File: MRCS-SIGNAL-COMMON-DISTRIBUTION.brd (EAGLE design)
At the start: 69 x 50 mm, 13 parts, among them CON1 DC PWR, CON2 DC PWR

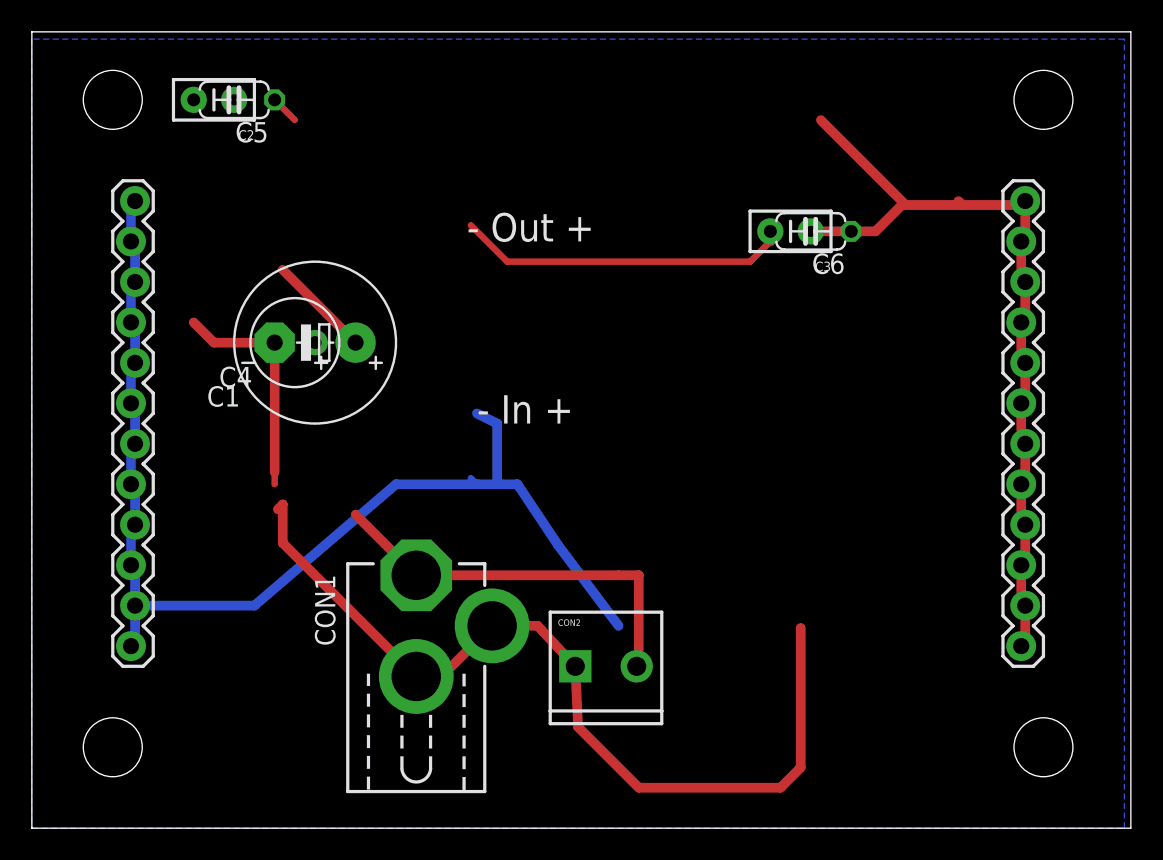
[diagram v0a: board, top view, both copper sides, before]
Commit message: initial board for testing
first pass, this is based on the Buckeroo footprint
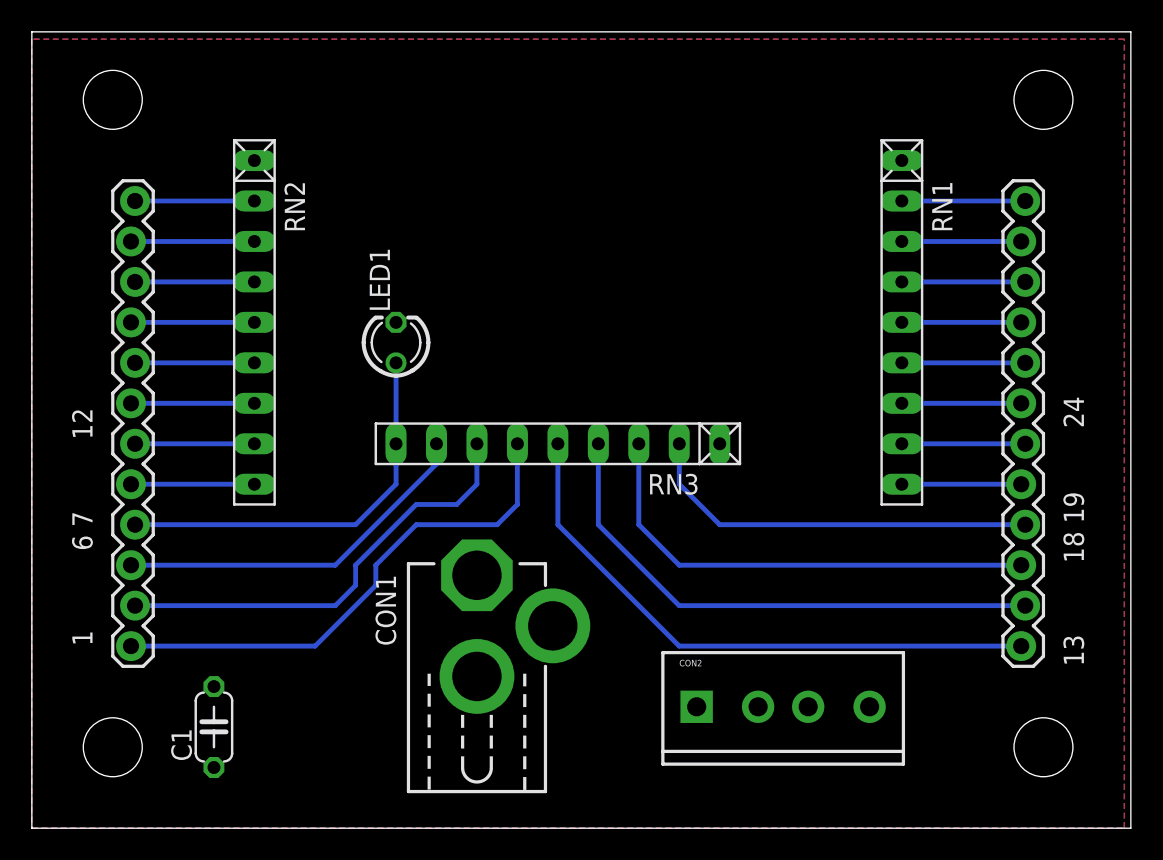
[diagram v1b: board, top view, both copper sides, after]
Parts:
- removed C2: 1.0uF@50, SPCoast:C-PTH-0.100
- removed C3: 10uF@50, SPCoast:C-PTH-0.100
- removed C4: 220uF @ 35V, SPCoast:E2.5-6
- removed C5: 1.0 UF@ 50V, SPCoast:C050-024X044
- removed C6: 10uF @ 50V, SPCoast:C050-024X044
- removed OUTPUT+: OUTPUT+, SPCoast:1X12_LOCK
- removed U$1: (no value), MRCS-prop65warningBtm:CA-PROP65WARNING
- removed U$3: (no value), MRCSLogoBtm:MRCSLOGOBTM
- added CON3: OUTPUT1, SPCoast:1X12_LOCK
- added LED1: RED, SPCoast:LED3MM
- added RN1, RN2, RN3: 270, resistor-net:RN-9
- C1: value 150uF@50 -> .01 uF; device SPCoast:E5-10.5 -> SPCoast:C050-024X044
- CON2: value DC PWR -> Power/GND; device SPCoast:SCREWTERMINAL-3.5MM-2_LOCK -> SPCoast:SCREWTERMINAL-3.5MM-4_LOCK
- CON4: value OUTPUT- -> OUTPUT2
- moved U$2 48.6 mm to (40.6, 39.4)
- moved C1 25.0 mm to (11.4, 6.35), turned to 90 degrees
- moved CON2 8.03 mm to (41.9, 7.62)
- moved CON1 3.81 mm to (27.9, 12.7)
- renumbered OUTPUT- to CON4
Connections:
- removed net OUTPUT+: C3.1, OUTPUT+.1, OUTPUT+.10, OUTPUT+.11, OUTPUT+.12, OUTPUT+.2, OUTPUT+.3, OUTPUT+.4, OUTPUT+.5, OUTPUT+.6, OUTPUT+.7, OUTPUT+.8, OUTPUT+.9
- new net N$10: CON4.11, RN2.3
- new net N$11: CON4.10, RN2.4
- new net N$12: CON4.9, RN2.5
- new net N$13: CON4.8, RN2.6
- new net N$14: CON4.7, RN2.7
- new net N$15: CON4.6, RN2.8
- new net N$16: CON4.5, RN2.9
- new net N$17: CON3.4, RN3.2
- new net N$18: CON3.3, RN3.3
- new net N$19: CON3.2, RN3.4
- new net N$20: CON3.1, RN3.5
- new net N$21: CON4.1, RN3.6
- new net N$22: CON4.4, LED1.A, RN3.9
- new net N$23: CON4.3, RN3.8
- new net N$24: CON4.2, RN3.7
- new net N$7: CON3.6, RN1.8
- net GND: now also C1.2, CON2.3, LED1.K; no longer C1.-, C3.2, CON4.1, CON4.10, CON4.11, CON4.12, CON4.2, CON4.3, CON4.4, CON4.5, CON4.6, CON4.7, CON4.8, CON4.9
- net INPUT+: now also C1.1, CON2.4, RN1.1, RN2.1
- net N$1: now also CON3.12, RN1.2; no longer C5.1
- net N$2: now also CON3.11, RN1.3; no longer C4.+
- net N$3: now also CON3.10, RN1.4; no longer C1.+
- net N$4: now also CON3.9, RN1.5; no longer C2.2
- net N$5: now also CON3.8, RN1.6; no longer C4.-
- net N$6: now also CON3.7, RN1.7; no longer C5.2
- net N$8: now also CON3.5, RN1.9; no longer C6.2
- net N$9: now also CON4.12, RN2.2; no longer C6.1
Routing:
- net GND: track 171.9 -> 0.00 mm
- net OUTPUT+: track 51.3 -> 0.00 mm
- net N$20: track 0.00 -> 37.3 mm
- net N$19: track 0.00 -> 34.0 mm
- net N$21: track 0.00 -> 32.5 mm
- net N$18: track 0.00 -> 30.3 mm
- net N$24: track 0.00 -> 27.9 mm
- net INPUT+: track 26.0 -> 0.00 mm
- net N$17: track 0.00 -> 25.3 mm
- net N$22: track 0.00 -> 25.1 mm
- net N$23: track 0.00 -> 23.1 mm
- net N$16: track 0.00 -> 7.75 mm
- net N$14: track 0.00 -> 7.75 mm
- net N$12: track 0.00 -> 7.75 mm
- net N$10: track 0.00 -> 7.75 mm
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- added copper zone on layer 16, net GND
- added copper zone on layer 1, net INPUT+
- removed copper zone on layer 16, net OUTOUT-
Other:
- board text added: "1 6 7 12"
- board text added: "13 18 19 24"
- board text added: "G + G +"
- board text added: "Signal Common Distribution Seth Neumann 20240126 V 1.0"
- board text removed: ""Buckeroo V1.6" Seth Neumann 20230226"
- board text removed: "+ V Jumper"
- board text removed: "- In +"
- board text removed: "- Out +"
- board text removed: "- V (GND) JUMP"
- board text removed: "C1"
- board text removed: "C2"
- board text removed: "C3"
- board text removed: "C4"
- board text removed: "C5"
- board text removed: "C6"
- board text removed: "CON1"
- board text removed: "CON2"
- board text removed: "GND"
- board text removed: "IN - +"
- board text removed: "MH-MINI-360"
- board text removed: "Output +"
- board text removed: "Output -"
- board text removed: "U$4"
- board text removed: "U$5"
- board text removed: "VR1"

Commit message: last minute fixes
added Prop 65 label and bottom logo
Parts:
- added U$1: (no value), MRCS-prop65warningBtm:CA-PROP65WARNING
- added U$3: (no value), MRCSLogoBtm:MRCSLOGOBTM
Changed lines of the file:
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@@
 <attribute name="NAME" x="15.875" y="40.64" size="1.27" layer="25" ratio="10" rot="R270"/>
 </element>
+<element name="U$1" library="MRCS-prop65warningBtm" package="CA-PROP65WARNING" value="" x="40.64" y="39.37"/>
+<element name="U$3" library="MRCSLogoBtm" package="MRCSLOGOBTM" value="" x="33.02" y="29.21"/>
 </elements>
 <signals>
